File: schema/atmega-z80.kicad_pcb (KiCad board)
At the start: 2 copper layers, 142.2 x 115.6 mm, 75 parts, among them J1 USB Connector, J2 Programmer ISP 10, J3 SPI Connector, J4 I2C Connector, Q1 PNP_2N4403, Q2 PNP_2N4403, Q3 NPN_2N4401, Q4 PNP_2N4403, U1 Z84C0010PEG, U2 ATmega324A-PU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

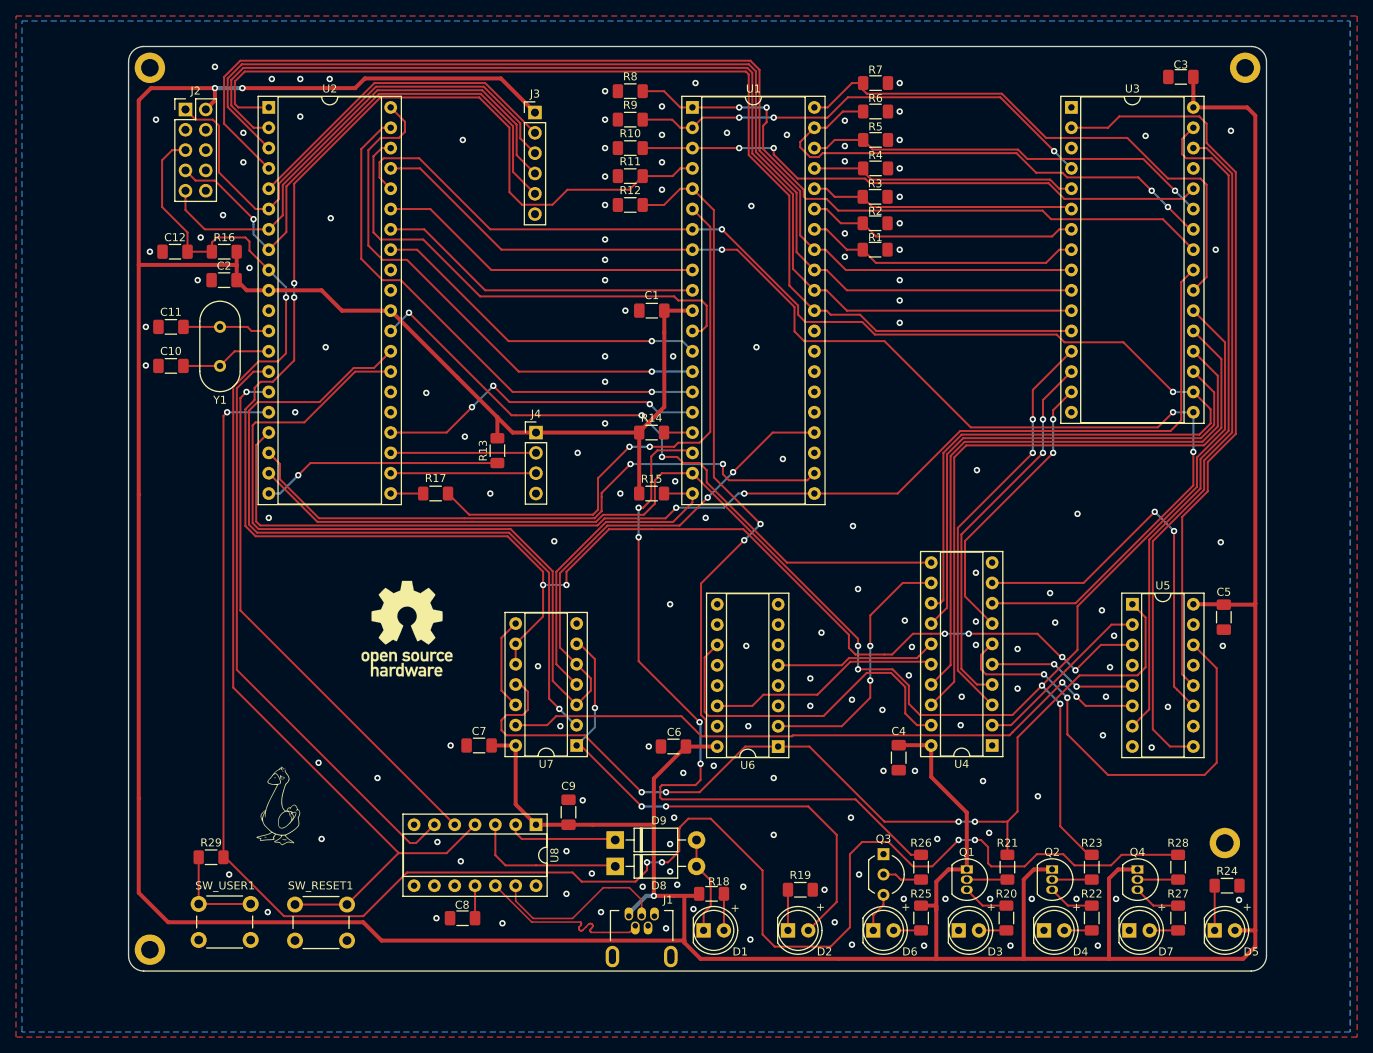
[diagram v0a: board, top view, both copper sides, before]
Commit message: PCB routing complete Minor improvements
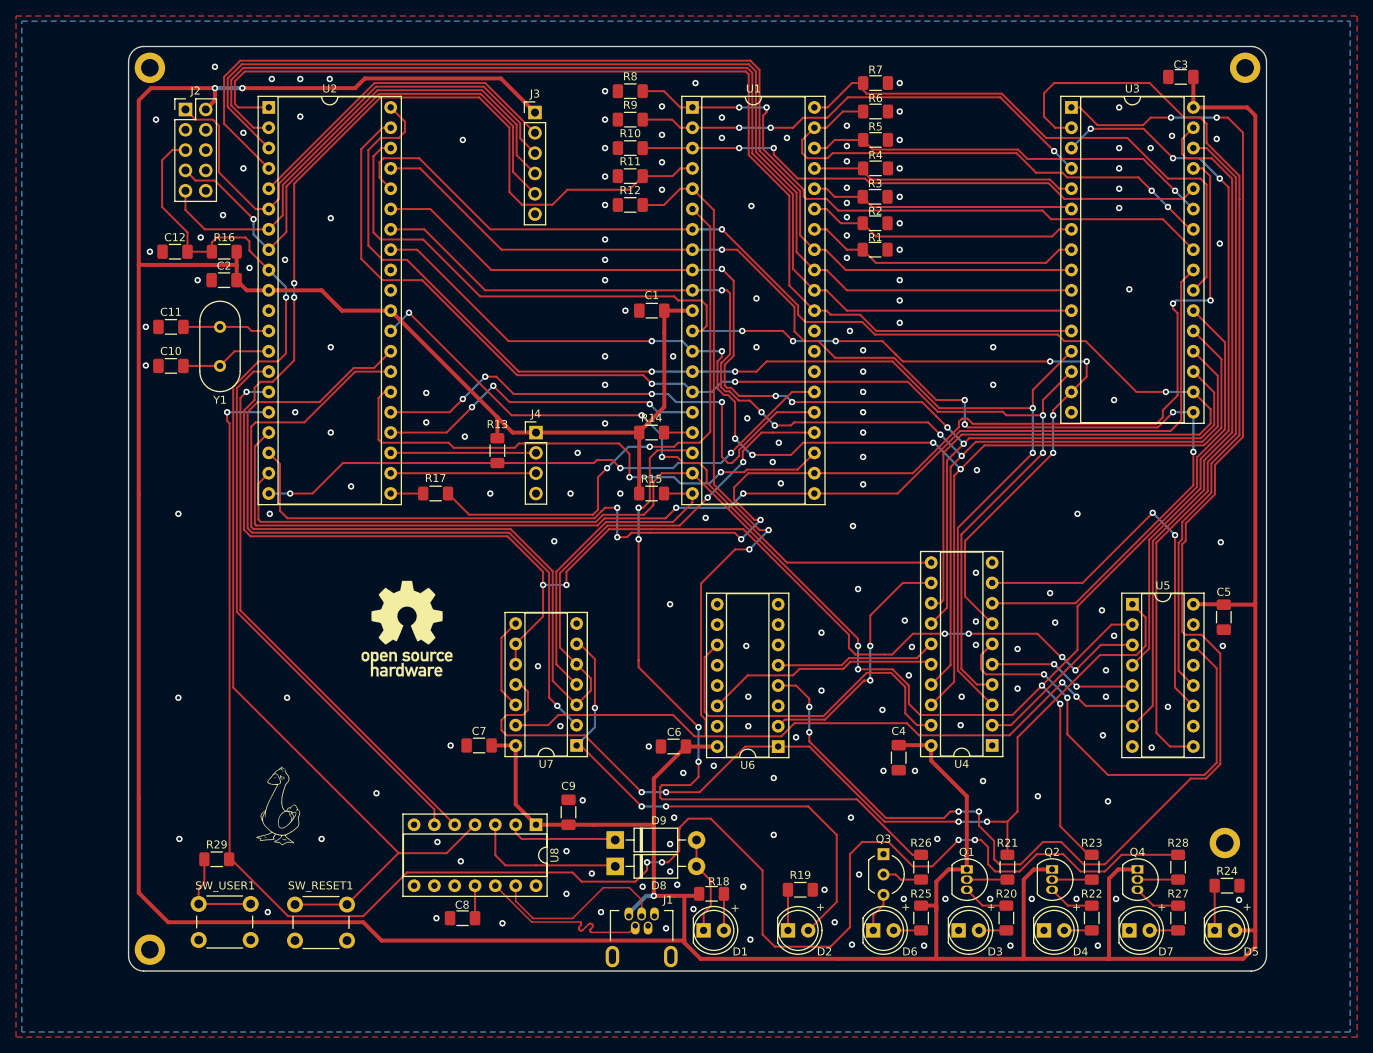
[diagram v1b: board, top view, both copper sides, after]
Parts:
- moved R29 0.75 mm to (82.8, 138.4)
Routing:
- net Net-(U3-Pad1): track 0.00 -> 187.0 mm, vias 0 -> 6
- net /#WR: track 78.6 -> 176.3 mm, vias 2 -> 6
- net Net-(U3-Pad3): track 0.00 -> 88.4 mm, vias 0 -> 3
- net /#BUSACK: track 0.00 -> 67.5 mm, vias 0 -> 2
- net /#BUSRQ: track 0.00 -> 66.4 mm, vias 0 -> 4
- net /D2: track 98.2 -> 153.6 mm, vias 2 -> 7
- net /D5: track 105.5 -> 157.3 mm, vias 0 -> 5
- net /D6: track 116.0 -> 166.2 mm, vias 0 -> 5
- net /D1: track 114.3 -> 160.4 mm, vias 3 -> 4
- net /D0: track 120.1 -> 165.6 mm, vias 3 -> 4
- net /D7: track 123.6 -> 169.1 mm, vias 1 -> 6
- net /#Z80_RESET: track 30.2 -> 74.3 mm, vias 1 -> 3
- net Net-(U3-Pad2): track 93.0 -> 106.0 mm
- net #MEM_LED: track 202.2 -> 207.4 mm
- net /ATMEGA_RX_AND_USB_TX: track 74.7 -> 69.6 mm
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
